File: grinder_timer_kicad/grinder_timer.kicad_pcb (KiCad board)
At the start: 2 copper layers, 29 parts, among them IC1 ATMEGA328P-P, T1 TRANS, U1 SSD1306_128x64OLED, U2 serial_to_usb, U3 LM7805CT

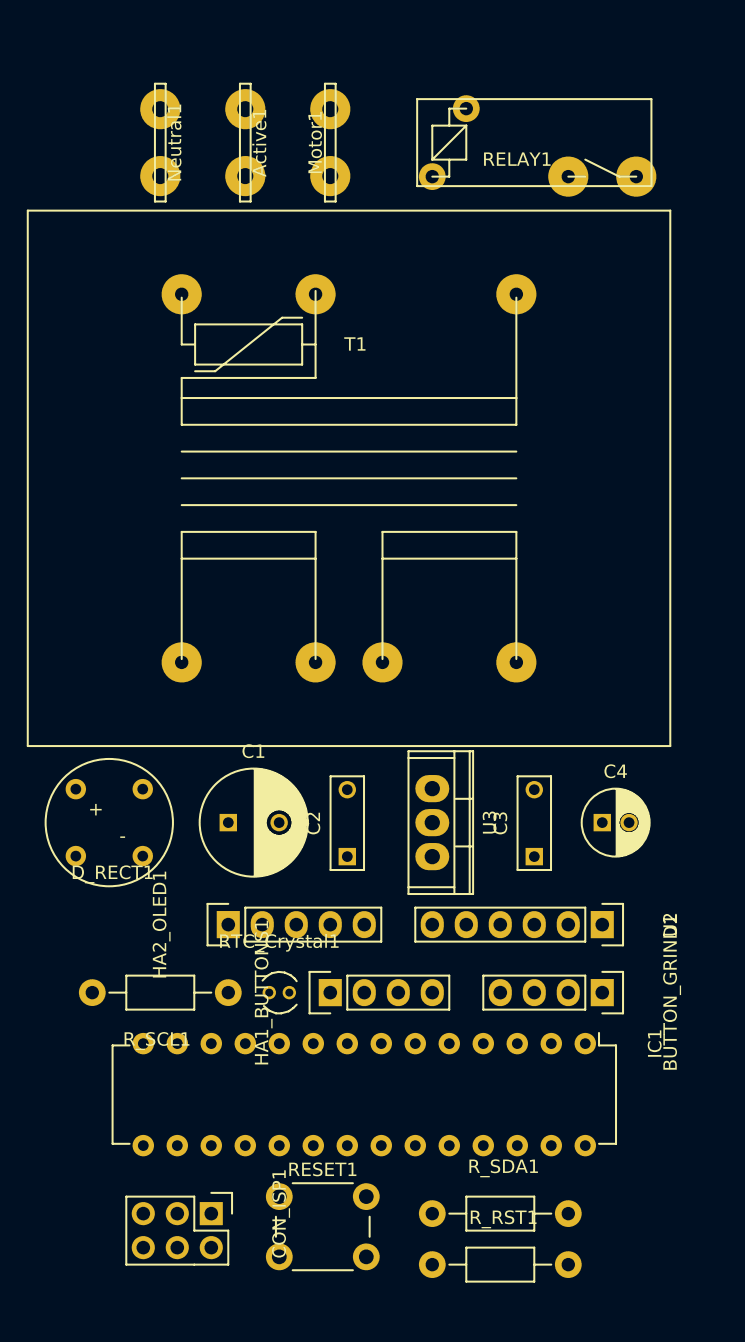
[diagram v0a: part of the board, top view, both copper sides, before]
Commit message: Work on the schematic.  Began PCB layout.
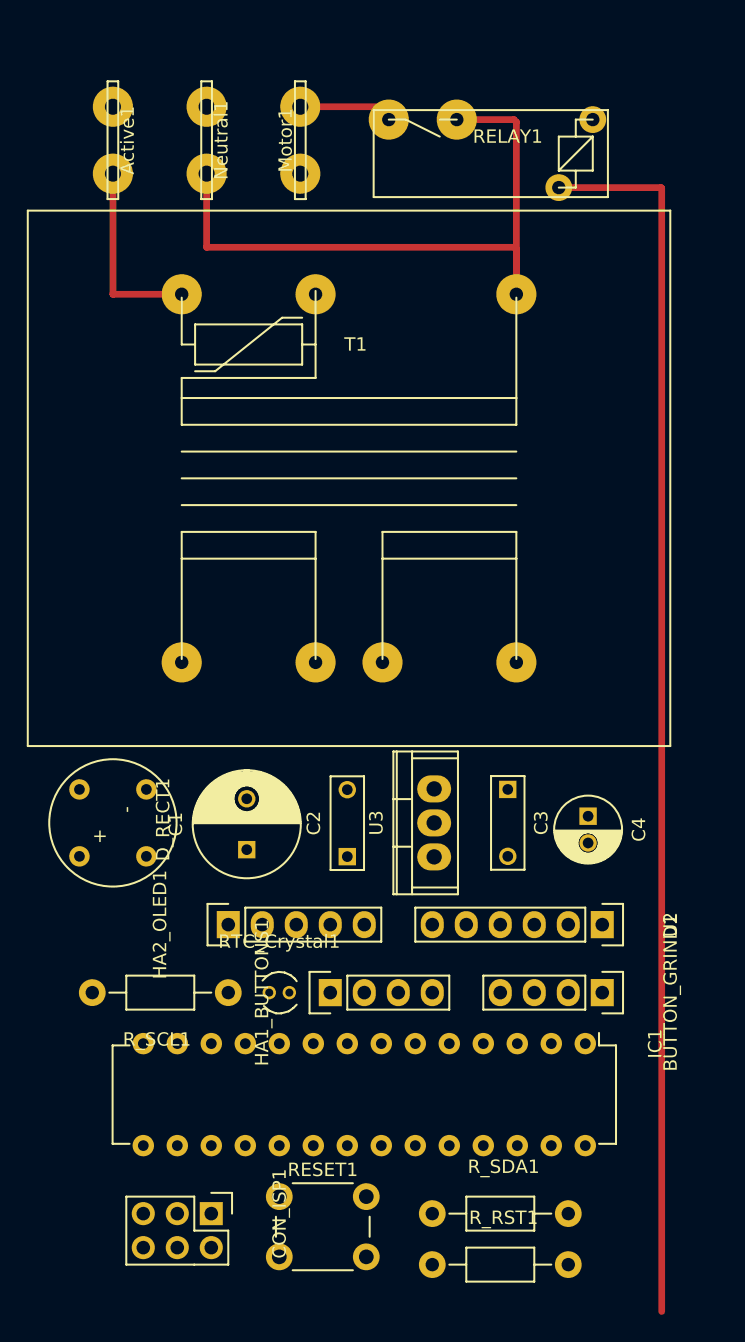
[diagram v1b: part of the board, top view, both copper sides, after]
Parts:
- moved Active1 9.89 mm to (62.5, 43.0)
- moved C3 5.40 mm to (92.0, 91.5), turned to 270 degrees
- moved Neutral1 3.46 mm to (69.5, 43.0)
- moved C1 2.45 mm to (72.5, 96.0), turned to 90 degrees
- moved Motor1 2.25 mm to (76.5, 43.0)
- moved C4 1.16 mm to (98.0, 93.5), turned to 270 degrees
- moved RELAY1 1.08 mm to (92.0, 44.0), turned to 180 degrees
- moved D_RECT1 0.27 mm to (62.5, 94.0), turned to 90 degrees
- moved U3 0.14 mm to (86.5, 94.0), turned to 90 degrees
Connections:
- RELAY1 pad A1: RELAY -> GND
- RELAY1 pad A2: GND -> RELAY
- T1 pad 1: Net-(Active1-Pad1) -> Net-(Neutral1-Pad1)
- T1 pad 3: Net-(Neutral1-Pad1) -> Net-(Active1-Pad1)
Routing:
- net GND: track 0.00 -> 91.6 mm
- net Net-(Neutral1-Pad1): track 0.00 -> 49.5 mm
- net Net-(Active1-Pad1): track 0.00 -> 14.1 mm
- net Net-(Motor1-Pad1): track 0.00 -> 7.51 mm
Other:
- net class Power added: clearance 0.2, trace_width 0.5, via_dia 0.6, via_drill 0.4

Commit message: PCB layout progress.
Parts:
- moved SW_DOWN1 75.2 mm to (244.0, 95.2), turned to 270 degrees
- moved SW_LEFT1 40.9 mm to (234.0, 85.2), turned to 180 degrees
- moved HB1_BUTTONS1 40.1 mm to (240.2, 85.2), turned to 90 degrees
- moved SW_RIGHT1 35.1 mm to (254.0, 85.2)
- moved SW_UP1 33.8 mm to (244.0, 75.2), turned to 90 degrees
- moved HB2_OLED1 27.9 mm to (239.0, 63.8), turned to 90 degrees
- moved U2 12.8 mm to (86.2, 101.8), turned to 90 degrees
- moved R_RST1 9.94 mm to (96.2, 126.0), turned to 180 degrees
- moved R_SCL1 9.62 mm to (61.5, 106.5), turned to 0 degrees
- moved R_SDA1 1.20 mm to (86.2, 122.0)
- moved U1 1.09 mm to (244.0, 67.5)
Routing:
- net +5V: track 0.00 -> 207.5 mm, vias 0 -> 8
- net GND: track 91.6 -> 261.0 mm, vias 0 -> 10
- net HA2_RESET: track 0.00 -> 128.6 mm
- net RELAY: track 0.00 -> 113.4 mm
- net GNDD: track 0.00 -> 104.8 mm
- net HA2_SDA: track 0.00 -> 61.4 mm
- net HA2_SCL: track 0.00 -> 58.3 mm
- net Net-(D_RECT1-Pad4): track 0.00 -> 55.2 mm
- net Net-(D_RECT1-Pad3): track 0.00 -> 49.0 mm
- net BUTTON_GRIND: track 0.00 -> 36.5 mm
- net Net-(C1-Pad1): track 0.00 -> 34.9 mm
- net AVR_RX: track 0.00 -> 29.0 mm
- net AVR_TX: track 0.00 -> 27.0 mm
- net Net-(HB1_BUTTONS1-Pad3): track 0.00 -> 21.3 mm
- net SCK: track 0.00 -> 15.4 mm
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- added copper zone on F.Cu, net GND

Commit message: Finished PCB layouts (first rev).
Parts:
- moved R_SCL1 183.4 mm to (239.0, 60.2)
- moved R_SDA1 166.0 mm to (239.0, 57.0)
- moved BUTTON_GRIND1 39.3 mm to (60.0, 102.0), turned to 90 degrees
- moved HA2_OLED1 30.6 mm to (94.8, 121.0), turned to 270 degrees
- moved R_RST1 14.4 mm to (85.0, 117.0), turned to 0 degrees
- moved RTC_Crystal1 5.80 mm to (71.5, 102.0)
- moved HA1_BUTTONS1 5.69 mm to (75.5, 102.0)
- moved CON_ISP1 5.20 mm to (69.5, 118.0)
- moved RESET1 5.01 mm to (74.0, 117.0)
- moved IC1 4.83 mm to (96.0, 106.0)
- moved U2 1.27 mm to (87.5, 102.0)
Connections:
- HB1_BUTTONS1 pad 1: Net-(HB1_BUTTONS1-Pad1) -> GNDD
- R_SCL1 pad 1: +5V -> HB2_SCL
- R_SCL1 pad 2: HA2_SCL -> +5VD
- R_SDA1 pad 1: +5V -> HB2_SDA
- R_SDA1 pad 2: HA2_SDA -> +5VD
- SW_UP1 pad 1: Net-(HB1_BUTTONS1-Pad1) -> GNDD
- SW_UP1 pad 3: Net-(HB1_BUTTONS1-Pad1) -> GNDD
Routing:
- net HA2_RESET: track 128.6 -> 63.5 mm
- net HA2_SDA: track 61.4 -> 12.1 mm
- net HA2_SCL: track 58.3 -> 18.7 mm
- net +5V: track 207.5 -> 168.9 mm, vias 8 -> 6
- net BUTTON_GRIND: track 36.5 -> 6.97 mm
- net AVR_RX: track 29.0 -> 5.57 mm
- net RELAY: track 113.4 -> 90.6 mm
- net AVR_TX: track 27.0 -> 13.1 mm
- net GNDD: track 104.8 -> 118.7 mm
- net Net-(HB1_BUTTONS1-Pad1): track 13.8 -> 0.00 mm
- net +5VD: track 7.35 -> 19.3 mm
- net HB2_SDA: track 7.64 -> 17.3 mm
- net HB2_SCL: track 7.62 -> 13.6 mm
- net GND: track 261.0 -> 256.8 mm, vias 10 -> 4
- net SCK: track 15.4 -> 13.3 mm
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- added copper zone on F.Cu, net GNDD
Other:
- board text added: "Clewsy_2017 grinder_timer"

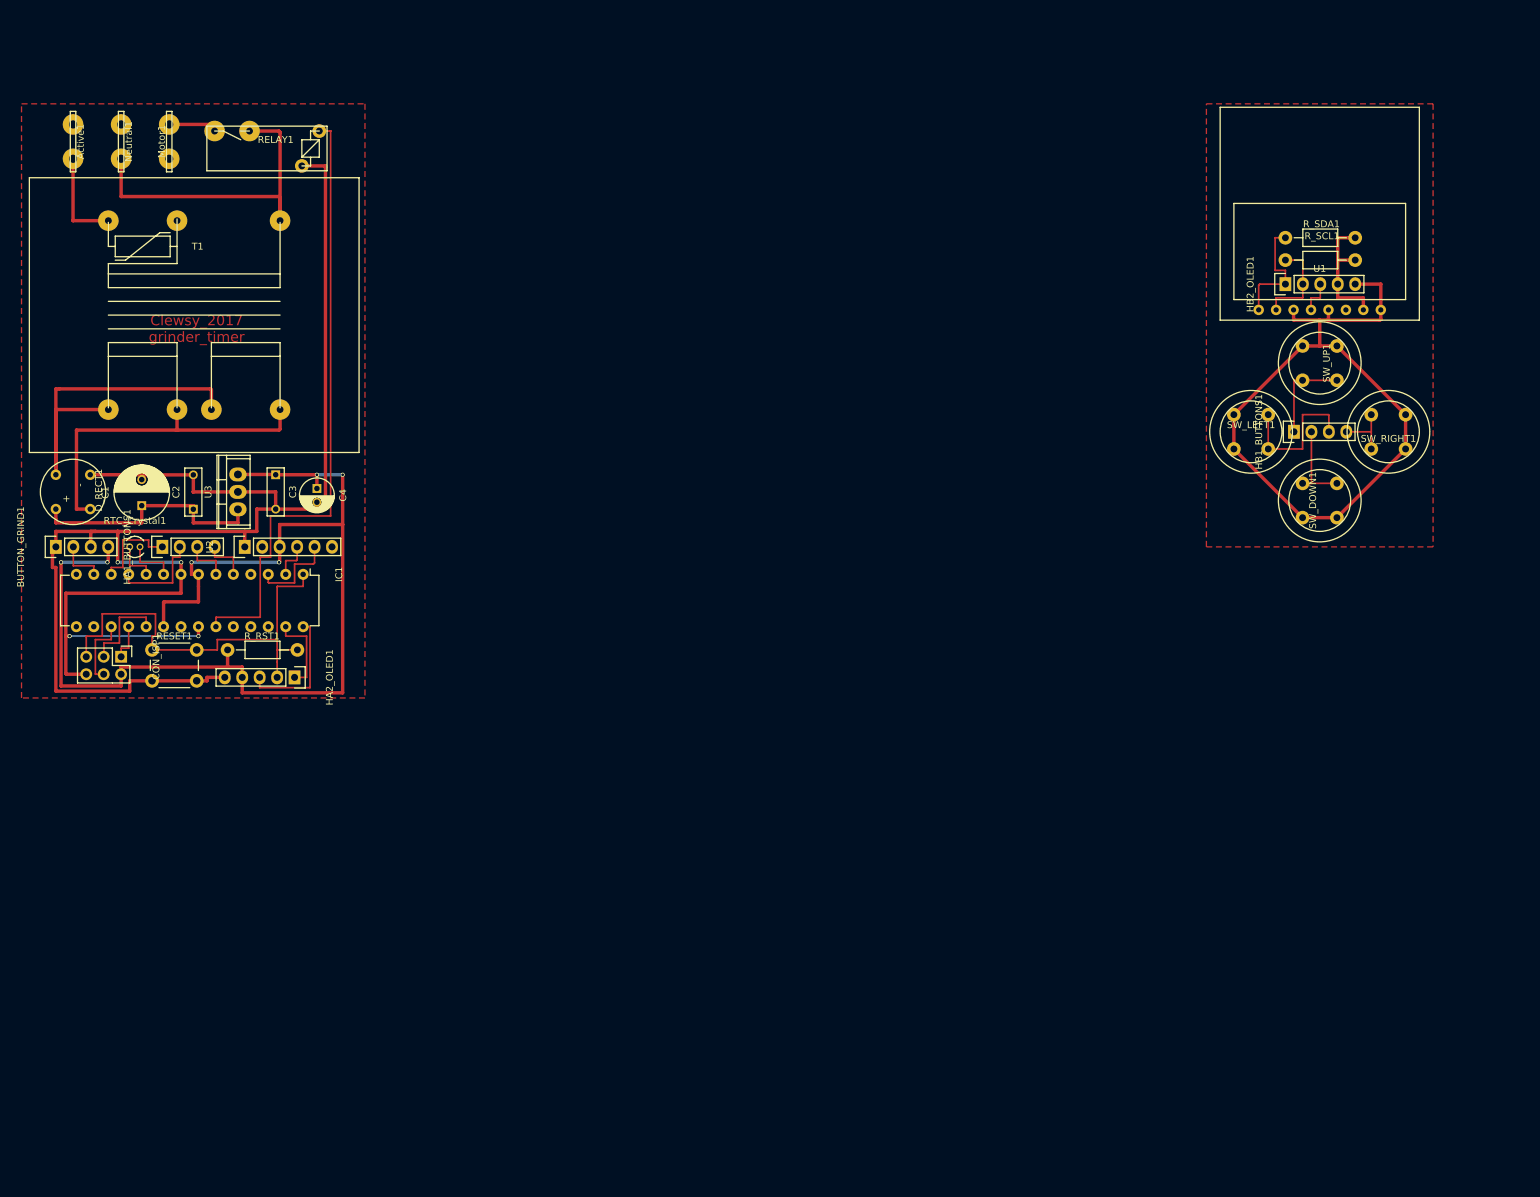
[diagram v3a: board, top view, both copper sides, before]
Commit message: Fixed a mis-wired push button on the schematic and PCB layout.
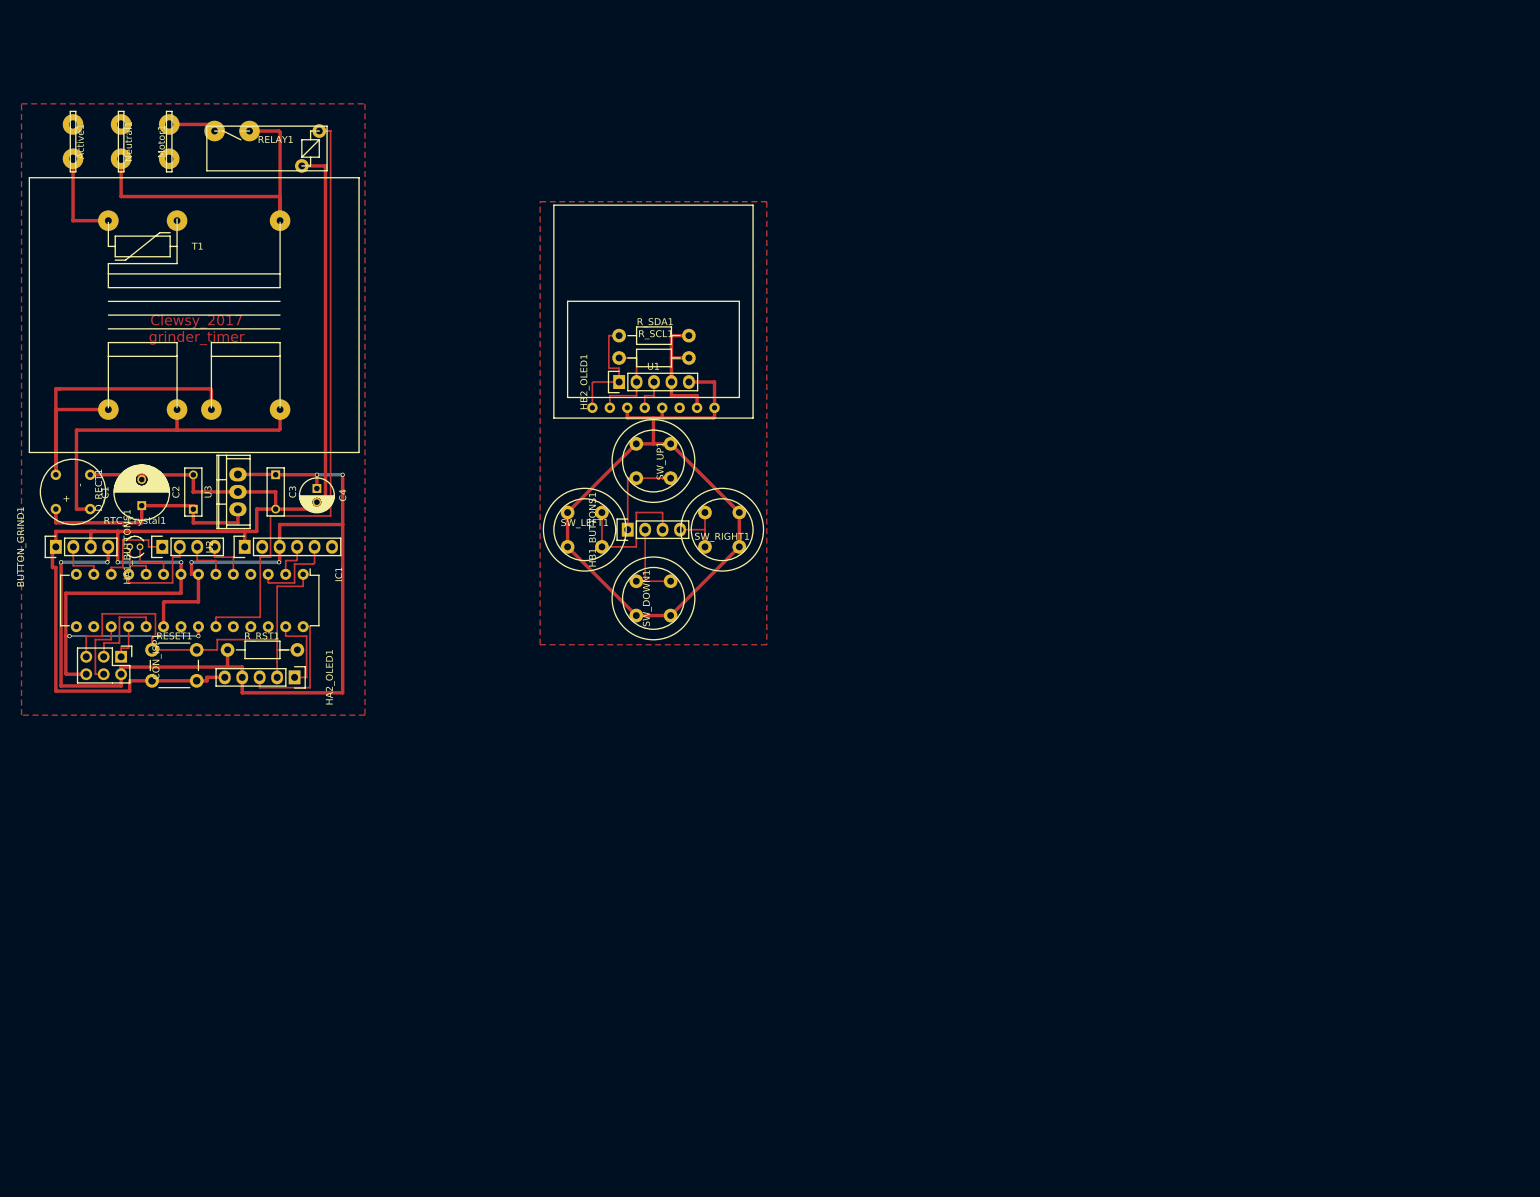
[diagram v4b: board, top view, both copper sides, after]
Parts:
- moved HB1_BUTTONS1 98.0 mm to (143.2, 99.5)
- moved HB2_OLED1 98.0 mm to (142.0, 78.0)
- moved R_SCL1 98.0 mm to (142.0, 74.5)
- moved R_SDA1 98.0 mm to (142.0, 71.2)
- moved SW_DOWN1 98.0 mm to (147.0, 109.5)
- moved SW_LEFT1 98.0 mm to (137.0, 99.5)
- moved SW_RIGHT1 98.0 mm to (157.0, 99.5)
- moved SW_UP1 98.0 mm to (147.0, 89.5)
- moved U1 98.0 mm to (147.0, 81.8)
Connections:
- HB1_BUTTONS1 pad 1: GNDD -> Net-(HB1_BUTTONS1-Pad1)
- SW_UP1 pad 1: GNDD -> Net-(HB1_BUTTONS1-Pad1)
- SW_UP1 pad 3: GNDD -> Net-(HB1_BUTTONS1-Pad1)
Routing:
- net Net-(HB1_BUTTONS1-Pad1): track 0.00 -> 13.8 mm
- net GNDD: track 118.7 -> 104.9 mm
